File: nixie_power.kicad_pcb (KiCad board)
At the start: 2 copper layers, 18 parts, among them J1 Screw_Terminal_01x02, J2 Screw_Terminal_01x02, Q1 2N7000, Q2 BC547, U1 LM555

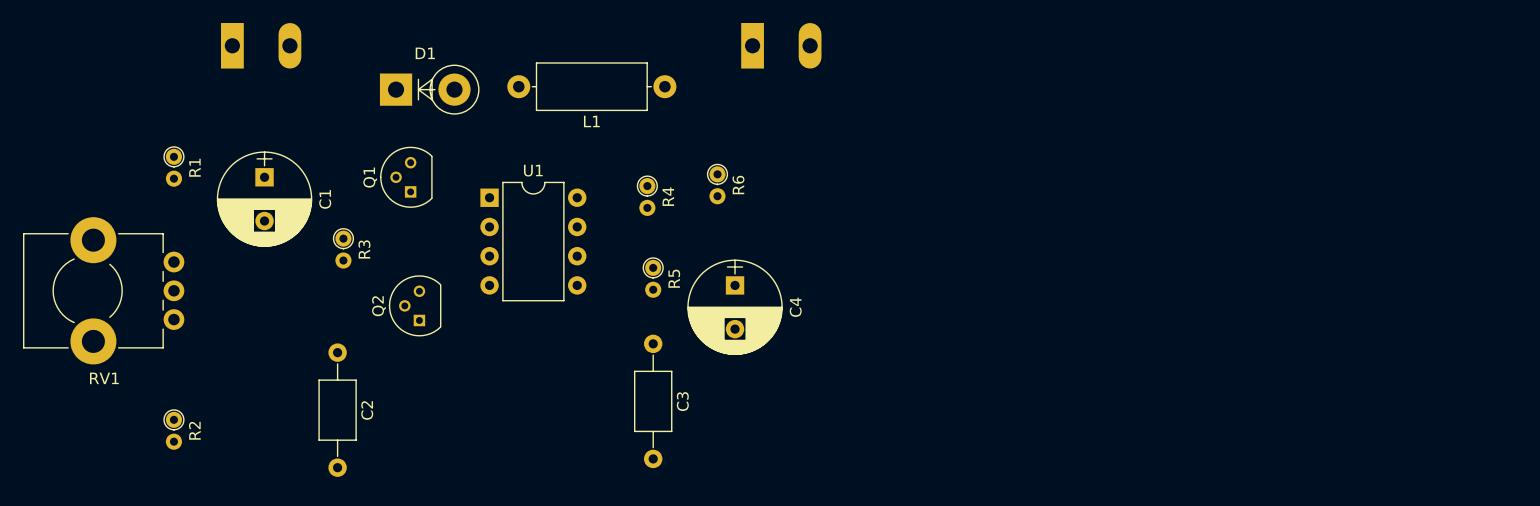
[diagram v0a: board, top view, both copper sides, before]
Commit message: オート配線をした
これから手動配線でジャンパワイヤに変更する
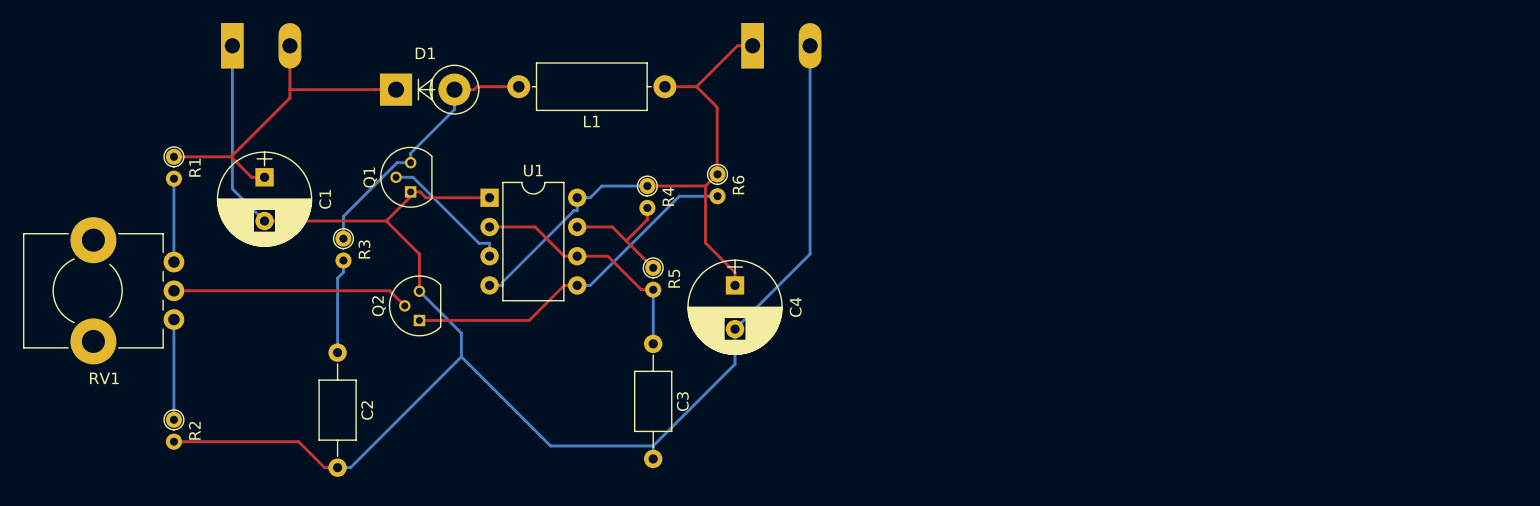
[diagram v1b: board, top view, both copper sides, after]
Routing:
- net Net-(C1-Pad2): track 0.00 -> 143.5 mm
- net Net-(C4-Pad1): track 0.00 -> 51.8 mm
- net Net-(Q2-Pad1): track 0.00 -> 30.4 mm
- net Net-(C1-Pad1): track 0.00 -> 29.6 mm
- net Net-(D1-Pad2): track 0.00 -> 23.3 mm
- net Net-(C3-Pad1): track 0.00 -> 21.2 mm
- net Net-(Q2-Pad2): track 0.00 -> 20.6 mm
- net Net-(R4-Pad2): track 0.00 -> 11.7 mm
- net Net-(Q1-Pad2): track 0.00 -> 11.6 mm
- net Net-(R2-Pad1): track 0.00 -> 8.72 mm
- net Net-(C2-Pad1): track 0.00 -> 8.22 mm
- net Net-(R1-Pad2): track 0.00 -> 7.24 mm
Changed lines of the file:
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@@
   (general
     (links 33)
-    (no_connects 33)
-    (area 142.652528 93.8786 162.676101 116.0286)
+    (no_connects 0)
+    (area 101.840999 80.175 177.016573 126.845001)
     (thickness 1.6)
     (drawings 0)
-    (tracks 0)
+    (tracks 90)
     (zones 0)
     (modules 18)
@@
     )
   )
+  (segment (start 123.19 100.33) (end 122.0647 100.33) (width 0.25) (layer F.Cu) (net 1))
+  (segment (start 115.316 98.552) (end 120.2867 98.552) (width 0.25) (layer F.Cu) (net 1))
+  (segment (start 120.2867 98.552) (end 122.0647 100.33) (width 0.25) (layer F.Cu) (net 1))
+  (segment (start 134.62 92.71) (end 132.8947 92.71) (width 0.25) (layer F.Cu) (net 1))
+  (segment (start 125.396 92.71) (end 132.8947 92.71) (width 0.25) (layer F.Cu) (net 1))
+  (segment (start 125.396 93.4427) (end 125.396 92.71) (width 0.25) (layer F.Cu) (net 1))
+  (segment (start 120.2867 98.552) (end 125.396 93.4427) (width 0.25) (layer F.Cu) (net 1))
+  (segment (start 125.396 92.71) (end 125.396 88.9) (width 0.25) (layer F.Cu) (net 1))
+  (segment (start 137.2233 102.108) (end 136.7153 101.6) (width 0.25) (layer F.Cu) (net 2))
+  (segment (start 142.748 102.108) (end 137.2233 102.108) (width 0.25) (layer F.Cu) (net 2))
+  (segment (start 135.89 101.6) (end 136.3027 101.6) (width 0.25) (layer F.Cu) (net 2))
+  (segment (start 136.3027 101.6) (end 136.7153 101.6) (width 0.25) (layer F.Cu) (net 2))
+  (segment (start 170.608 107.004) (end 164.084 113.528) (width 0.25) (layer B.Cu) (net 2))
+  (segment (start 170.608 88.9) (end 170.608 107.004) (width 0.25) (layer B.Cu) (net 2))
+  (segment (start 120.396 101.336) (end 123.19 104.13) (width 0.25) (layer B.Cu) (net 2))
+  (segment (start 120.396 88.9) (end 120.396 101.336) (width 0.25) (layer B.Cu) (net 2))
+  (segment (start 164.084 116.5707) (end 164.084 113.528) (width 0.25) (layer B.Cu) (net 2))
+  (segment (start 156.972 123.6827) (end 164.084 116.5707) (width 0.25) (layer B.Cu) (net 2))
+  (segment (start 156.972 124.808) (end 156.972 123.6827) (width 0.25) (layer B.Cu) (net 2))
+  (segment (start 136.652 107.0093) (end 136.652 110.236) (width 0.25) (layer F.Cu) (net 2))
+  (segment (start 133.7727 104.13) (end 136.652 107.0093) (width 0.25) (layer F.Cu) (net 2))
+  (segment (start 136.3027 101.6) (end 133.7727 104.13) (width 0.25) (layer F.Cu) (net 2))
+  (segment (start 133.7727 104.13) (end 123.19 104.13) (width 0.25) (layer F.Cu) (net 2))
+  (segment (start 126.1567 123.312) (end 128.4147 125.57) (width 0.25) (layer F.Cu) (net 2))
+  (segment (start 115.316 123.312) (end 126.1567 123.312) (width 0.25) (layer F.Cu) (net 2))
+  (segment (start 129.54 125.57) (end 128.4147 125.57) (width 0.25) (layer F.Cu) (net 2))
+  (segment (start 129.54 125.57) (end 130.6653 125.57) (width 0.25) (layer B.Cu) (net 2))
+  (segment (start 140.3019 113.8859) (end 140.3019 115.9334) (width 0.25) (layer B.Cu) (net 2))
+  (segment (start 136.652 110.236) (end 140.3019 113.8859) (width 0.25) (layer B.Cu) (net 2))
+  (segment (start 148.0512 123.6827) (end 140.3019 115.9334) (width 0.25) (layer B.Cu) (net 2))
+  (segment (start 156.972 123.6827) (end 148.0512 123.6827) (width 0.25) (layer B.Cu) (net 2))
+  (segment (start 140.3019 115.9334) (end 130.6653 125.57) (width 0.25) (layer B.Cu) (net 2))
+  (segment (start 129.54 109.0973) (end 129.54 115.57) (width 0.25) (layer B.Cu) (net 3))
+  (segment (start 130.048 108.5893) (end 129.54 109.0973) (width 0.25) (layer B.Cu) (net 3))
+  (segment (start 130.048 107.564) (end 130.048 108.5893) (width 0.25) (layer B.Cu) (net 3))
+  (segment (start 156.972 110.104) (end 155.9467 110.104) (width 0.25) (layer F.Cu) (net 4))
+  (segment (start 156.972 110.104) (end 156.972 114.808) (width 0.25) (layer B.Cu) (net 4))
+  (segment (start 153.0307 107.188) (end 150.368 107.188) (width 0.25) (layer F.Cu) (net 4))
+  (segment (start 155.9467 110.104) (end 153.0307 107.188) (width 0.25) (layer F.Cu) (net 4))
+  (segment (start 146.7027 104.648) (end 142.748 104.648) (width 0.25) (layer F.Cu) (net 4))
+  (segment (start 149.2427 107.188) (end 146.7027 104.648) (width 0.25) (layer F.Cu) (net 4))
+  (segment (start 150.368 107.188) (end 149.2427 107.188) (width 0.25) (layer F.Cu) (net 4))
+  (segment (start 150.368 102.108) (end 151.4933 102.108) (width 0.25) (layer B.Cu) (net 5))
+  (segment (start 150.0867 103.2333) (end 150.368 103.2333) (width 0.25) (layer B.Cu) (net 5))
+  (segment (start 143.8733 109.4467) (end 150.0867 103.2333) (width 0.25) (layer B.Cu) (net 5))
+  (segment (start 143.8733 109.728) (end 143.8733 109.4467) (width 0.25) (layer B.Cu) (net 5))
+  (segment (start 142.748 109.728) (end 143.8733 109.728) (width 0.25) (layer B.Cu) (net 5))
+  (segment (start 150.368 102.108) (end 150.368 103.2333) (width 0.25) (layer B.Cu) (net 5))
+  (segment (start 152.5093 101.092) (end 156.464 101.092) (width 0.25) (layer B.Cu) (net 5))
+  (segment (start 151.4933 102.108) (end 152.5093 101.092) (width 0.25) (layer B.Cu) (net 5))
+  (segment (start 165.608 88.9) (end 164.2927 88.9) (width 0.25) (layer F.Cu) (net 5))
+  (segment (start 164.084 109.728) (end 164.084 108.6027) (width 0.25) (layer F.Cu) (net 5))
+  (segment (start 156.464 101.092) (end 161.5162 101.092) (width 0.25) (layer F.Cu) (net 5))
+  (segment (start 161.5162 106.0349) (end 164.084 108.6027) (width 0.25) (layer F.Cu) (net 5))
+  (segment (start 161.5162 101.092) (end 161.5162 106.0349) (width 0.25) (layer F.Cu) (net 5))
+  (segment (start 164.2927 88.9) (end 160.7367 92.456) (width 0.25) (layer F.Cu) (net 5))
+  (segment (start 160.7367 92.456) (end 157.988 92.456) (width 0.25) (layer F.Cu) (net 5))
+  (segment (start 162.5322 94.2515) (end 160.7367 92.456) (width 0.25) (layer F.Cu) (net 5))
+  (segment (start 162.5322 100.076) (end 162.5322 94.2515) (width 0.25) (layer F.Cu) (net 5))
+  (segment (start 162.56 100.076) (end 162.5322 100.076) (width 0.25) (layer F.Cu) (net 5))
+  (segment (start 162.5322 100.076) (end 161.5162 101.092) (width 0.25) (layer F.Cu) (net 5))
+  (segment (start 139.7 92.71) (end 139.7 94.4353) (width 0.25) (layer B.Cu) (net 6))
+  (segment (start 135.89 98.2453) (end 139.7 94.4353) (width 0.25) (layer B.Cu) (net 6))
+  (segment (start 135.89 99.06) (end 135.89 98.2453) (width 0.25) (layer B.Cu) (net 6))
+  (segment (start 141.6793 92.456) (end 141.4253 92.71) (width 0.25) (layer F.Cu) (net 6))
+  (segment (start 145.288 92.456) (end 141.6793 92.456) (width 0.25) (layer F.Cu) (net 6))
+  (segment (start 139.7 92.71) (end 141.4253 92.71) (width 0.25) (layer F.Cu) (net 6))
+  (segment (start 134.7205 99.06) (end 135.89 99.06) (width 0.25) (layer B.Cu) (net 6))
+  (segment (start 130.048 103.7325) (end 134.7205 99.06) (width 0.25) (layer B.Cu) (net 6))
+  (segment (start 130.048 105.664) (end 130.048 103.7325) (width 0.25) (layer B.Cu) (net 6))
+  (segment (start 136.0908 100.33) (end 134.62 100.33) (width 0.25) (layer B.Cu) (net 7))
+  (segment (start 141.8235 106.0627) (end 136.0908 100.33) (width 0.25) (layer B.Cu) (net 7))
+  (segment (start 142.748 106.0627) (end 141.8235 106.0627) (width 0.25) (layer B.Cu) (net 7))
+  (segment (start 142.748 107.188) (end 142.748 106.0627) (width 0.25) (layer B.Cu) (net 7))
+  (segment (start 134.072 110.196) (end 135.382 111.506) (width 0.25) (layer F.Cu) (net 8))
+  (segment (start 115.316 110.196) (end 134.072 110.196) (width 0.25) (layer F.Cu) (net 8))
+  (segment (start 146.1947 112.776) (end 136.652 112.776) (width 0.25) (layer F.Cu) (net 9))
+  (segment (start 149.2427 109.728) (end 146.1947 112.776) (width 0.25) (layer F.Cu) (net 9))
+  (segment (start 150.368 109.728) (end 149.2427 109.728) (width 0.25) (layer F.Cu) (net 9))
+  (segment (start 159.2453 101.976) (end 162.56 101.976) (width 0.25) (layer B.Cu) (net 9))
+  (segment (start 151.4933 109.728) (end 159.2453 101.976) (width 0.25) (layer B.Cu) (net 9))
+  (segment (start 150.368 109.728) (end 151.4933 109.728) (width 0.25) (layer B.Cu) (net 9))
+  (segment (start 115.316 107.696) (end 115.316 100.452) (width 0.25) (layer B.Cu) (net 10))
+  (segment (start 115.316 112.696) (end 115.316 121.412) (width 0.25) (layer B.Cu) (net 11))
+  (segment (start 150.368 104.648) (end 151.3807 104.648) (width 0.25) (layer F.Cu) (net 12))
+  (segment (start 156.464 102.992) (end 156.464 104.0173) (width 0.25) (layer F.Cu) (net 12))
+  (segment (start 154.6247 105.8566) (end 156.464 104.0173) (width 0.25) (layer F.Cu) (net 12))
+  (segment (start 153.416 104.648) (end 154.6247 105.8566) (width 0.25) (layer F.Cu) (net 12))
+  (segment (start 151.3807 104.648) (end 153.416 104.648) (width 0.25) (layer F.Cu) (net 12))
+  (segment (start 154.6247 105.8566) (end 156.972 108.204) (width 0.25) (layer F.Cu) (net 12))
 )

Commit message: 穴の開け方を変更した
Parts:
- moved R3 62.0 mm to (192.0, 107.7), turned to 180 degrees
- moved Q1 60.5 mm to (196.3, 102.1)
- moved Q2 60.5 mm to (197.1, 113.3)
- moved J1 60.5 mm to (180.8, 89.4)
- moved C1 60.5 mm to (183.6, 100.8)
- moved C2 60.5 mm to (190.0, 116.1)
- moved C3 60.5 mm to (217.4, 115.3)
- moved C4 60.5 mm to (224.5, 110.2)
- moved D1 60.5 mm to (195.1, 93.2)
- moved J2 60.5 mm to (226.1, 89.4)
- moved L1 60.5 mm to (218.4, 93.0)
- moved R1 60.5 mm to (175.8, 99.1)
- moved R2 60.5 mm to (175.8, 121.9)
- moved R4 60.5 mm to (216.9, 101.6)
- moved R5 60.5 mm to (217.4, 108.7)
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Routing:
- net Net-(C1-Pad2): track 143.5 -> 160.4 mm, vias 0 -> 4
- net Net-(D1-Pad2): track 23.3 -> 28.3 mm, vias 0 -> 2
- net Net-(Q1-Pad2): track 11.6 -> 15.3 mm, vias 0 -> 2
- net Net-(C4-Pad1): track 51.8 -> 55.4 mm, vias 0 -> 2
- net Net-(Q2-Pad1): track 30.4 -> 31.6 mm, vias 0 -> 2
- net Net-(C2-Pad1): track 8.22 -> 8.44 mm, vias 0 -> 2
